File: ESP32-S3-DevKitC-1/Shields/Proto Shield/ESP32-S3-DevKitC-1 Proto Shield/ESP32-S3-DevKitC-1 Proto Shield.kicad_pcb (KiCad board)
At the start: 2 copper layers, 48.3 x 83.8 mm, 0 parts

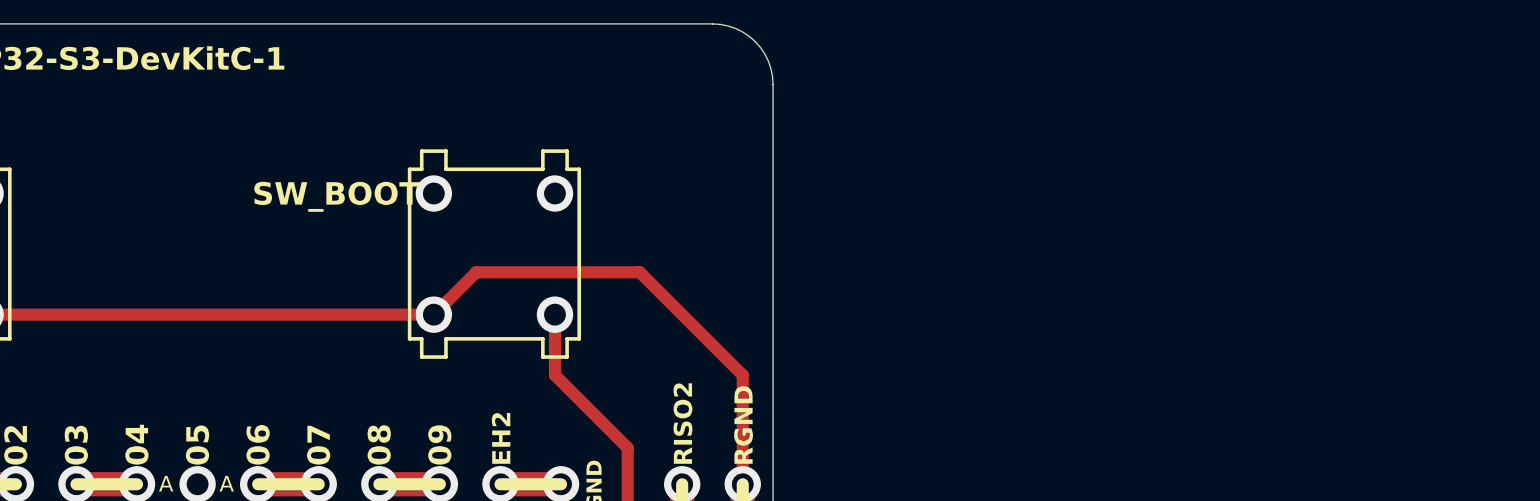
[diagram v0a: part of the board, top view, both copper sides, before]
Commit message: NFC reader board version submitted to JLCPCB
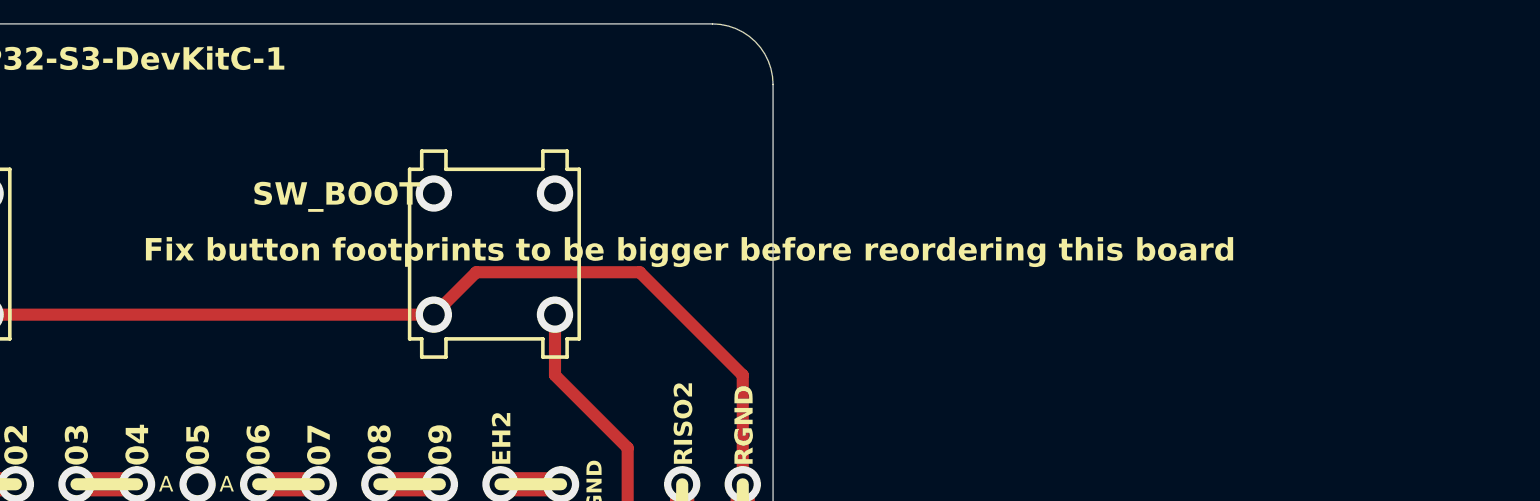
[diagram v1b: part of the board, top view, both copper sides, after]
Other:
- board text added: "Fix button footprints to be bigger before reordering this board"
- board text added: "M/N: JDS2.COM/AAB/001"
- board text added: "VER: 01.00.00"
- board text removed: "locked"
